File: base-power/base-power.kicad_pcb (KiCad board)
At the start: 2 copper layers, 4 parts

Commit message: Add current sensor, RTC battery, Power protection
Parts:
- removed the P at (52.1, 97.8)
- added 500 mA AC: V***, 2PIN_6mm, F.Cu at (78.7, 87.6)
- added ?: Val**, PIN_ARRAY_1, F.Cu at (99.1, 148.6)
- added Common Choke: VAL**, TRANSF-MICRO, F.Cu at (119.4, 101.6)
- added FUSE: 1,25 A, D3, F.Cu at (100.3, 121.9)
- added INA219: Val**, PIN_ARRAY_5x1, F.Cu at (99.1, 141.0)
- added P: POWER BOARD, VASCH8x2, F.Cu at (363.2, 212.1)
- added P***: BORN2, bornier2, F.Cu at (49.5, 92.7)
- added Power bypass: Val**, PIN_ARRAY_2X1, F.Cu at (95.2, 147.3)
- moved VARISTORE 19.3 mm to (74.9, 115.6), turned to 0 degrees
- moved LD1086 14.2 mm to (76.2, 137.2)
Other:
- board text added: "Gnd"
- board text added: "SCA0"
- board text added: "SCL0"
- board text added: "Scl"
- board text added: "Sda"
- board text added: "Vcc"
- board text added: "Vin+"
- board text added: "Vin-"

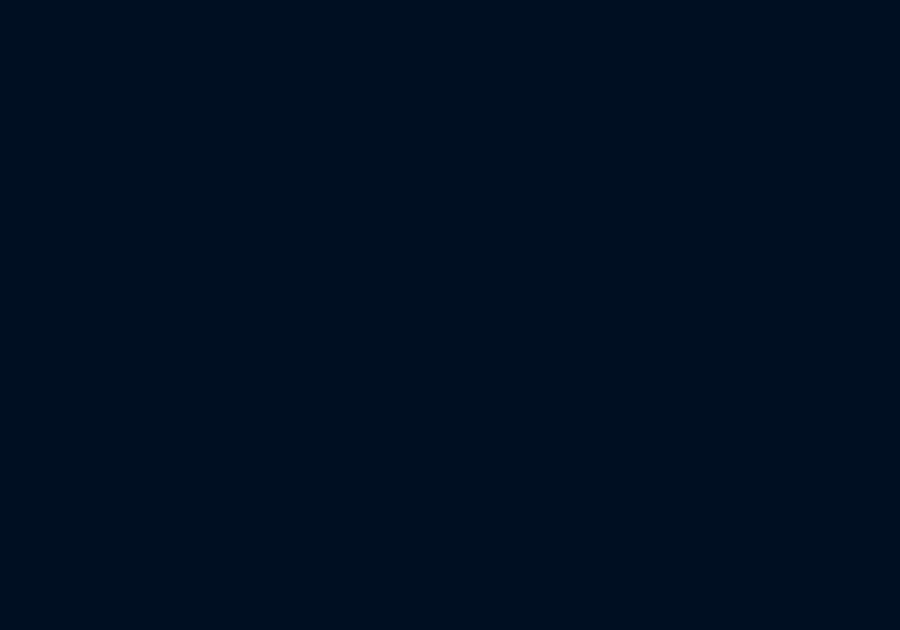
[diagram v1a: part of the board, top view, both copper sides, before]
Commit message: Power revision and add ina219 sensor
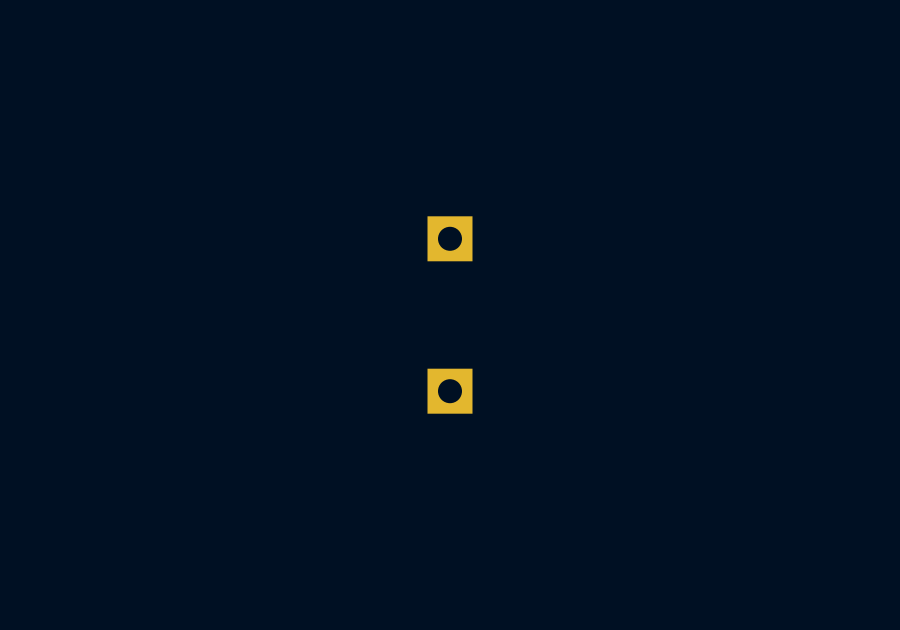
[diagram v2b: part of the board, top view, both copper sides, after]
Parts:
- added AD0: Val**, SIL-1, F.Cu at (340.4, 191.8)
- added AD1: Val**, SIL-1, F.Cu at (340.4, 196.8)
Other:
- board text added: "AD0"
- board text added: "AD1"
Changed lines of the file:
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@@
     (area 43.2816 24.079999 396.290001 262.940001)
     (thickness 1.6)
-    (drawings 21)
+    (drawings 23)
     (tracks 0)
     (zones 0)
-    (modules 11)
+    (modules 13)
     (nets 1)
   )
@@
     (visible_elements FFFFFBBF)
     (pcbplotparams
-      (layerselection 270532608)
+      (layerselection 270565376)
       (usegerberextensions false)
       (excludeedgelayer false)
@@
       (hpglpenoverlay 2)
       (psnegative false)
-      (psa4output false)
+      (psa4output true)
       (plotreference true)
       (plotvalue true)
@@
     (uvia_drill 0.127)
     (add_net "")
+  )
+  (module SIL-1 (layer "Rame Fronte")
+    (at 340.36 196.85)
+    (descr "Connecteurs 1 pin")
+    (tags "CONN DEV")
+    (fp_text reference AD1 (at 0 -1.7) (layer "Serigrafia Fronte")
+      (effects (font (size 0.8 0.8) (thickness 0.15)))
+    )
+    (fp_text value Val** (at 0.1 -1.7) (layer "Serigrafia Fronte") hide
+      (effects (font (size 0.8 0.8) (thickness 0.15)))
+    )
+    (fp_line (start -0.9 -0.9) (end 0.9 -0.9) (layer "Serigrafia Fronte") (width 0.15))
+    (fp_line (start 0.9 -0.9) (end 0.9 0.9) (layer "Serigrafia Fronte") (width 0.15))
+    (fp_line (start 0.9 0.9) (end -0.9 0.9) (layer "Serigrafia Fronte") (width 0.15))
+    (fp_line (start -0.9 0.9) (end -0.9 -0.9) (layer "Serigrafia Fronte") (width 0.15))
+    (pad 1 thru_hole rect (at 0 0) (size 1.5 1.5) (drill 0.8)
+      (layers *.Cu *.Mask "Serigrafia Fronte")
+    )
   )
   (module bornier4 (layer "Rame Fronte")
@@
     )
   )
+  (module SIL-1 (layer "Rame Fronte")
+    (at 340.36 191.77)
+    (descr "Connecteurs 1 pin")
+    (tags "CONN DEV")
+    (fp_text reference AD0 (at 0 -1.7) (layer "Serigrafia Fronte")
+      (effects (font (size 0.8 0.8) (thickness 0.15)))
+    )
+    (fp_text value Val** (at 0.1 -1.7) (layer "Serigrafia Fronte") hide
+      (effects (font (size 0.8 0.8) (thickness 0.15)))
+    )
+    (fp_line (start -0.9 -0.9) (end 0.9 -0.9) (layer "Serigrafia Fronte") (width 0.15))
+    (fp_line (start 0.9 -0.9) (end 0.9 0.9) (layer "Serigrafia Fronte") (width 0.15))
+    (fp_line (start 0.9 0.9) (end -0.9 0.9) (layer "Serigrafia Fronte") (width 0.15))
+    (fp_line (start -0.9 0.9) (end -0.9 -0.9) (layer "Serigrafia Fronte") (width 0.15))
+    (pad 1 thru_hole rect (at 0 0) (size 1.5 1.5) (drill 0.8)
+      (layers *.Cu *.Mask "Serigrafia Fronte")
+    )
+  )
+  (gr_text AD1 (at 372.11 205.74) (layer "Serigrafia Fronte")
+    (effects (font (size 1.5 1.5) (thickness 0.3)))
+  )
+  (gr_text AD0 (at 354.33 205.74) (layer "Serigrafia Fronte")
+    (effects (font (size 1.5 1.5) (thickness 0.3)))
+  )
   (gr_text SCL0 (at 354.33 203.2) (layer "Serigrafia Fronte")

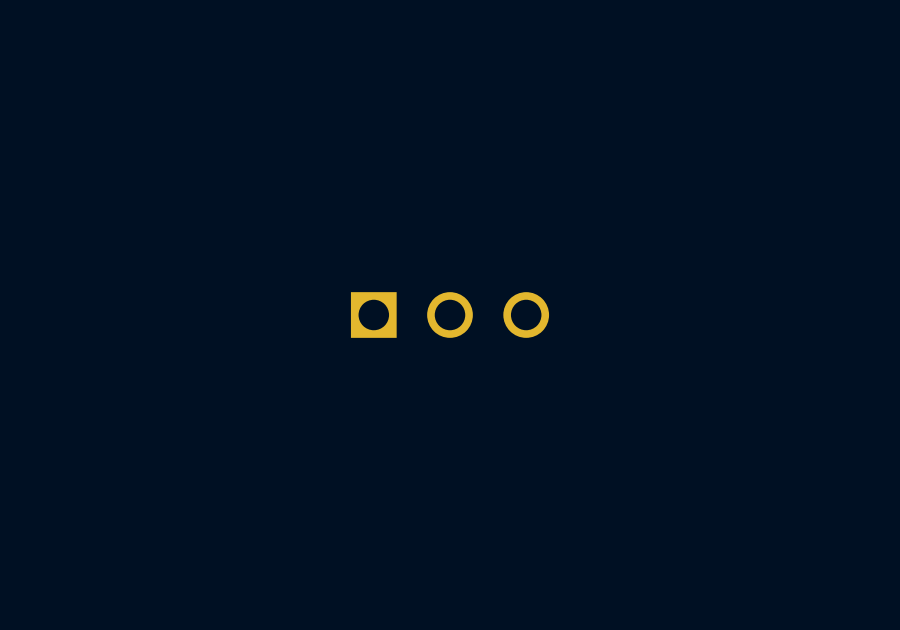
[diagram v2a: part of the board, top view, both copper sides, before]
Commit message: Fix Power schematics
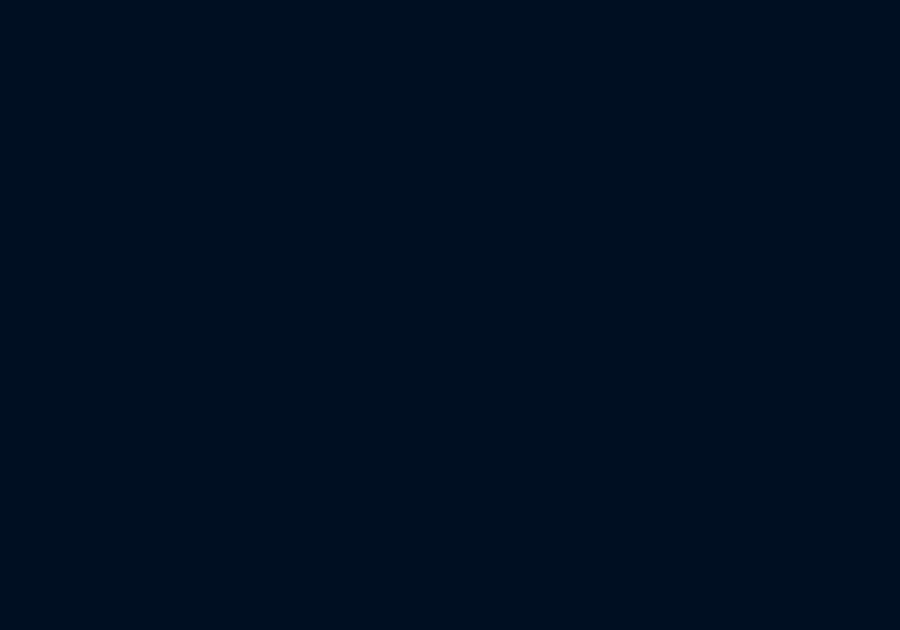
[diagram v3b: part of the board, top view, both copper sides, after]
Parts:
- removed LD1086: Val**, PIN_ARRAY_3X1
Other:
- board text added: "GND 3,3V NC 5V"
- board text removed: "GND 3,3V 3,6V 5V"
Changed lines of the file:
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@@
     (tracks 0)
     (zones 0)
-    (modules 13)
+    (modules 12)
     (nets 1)
   )
@@
     )
   )
-  (module PIN_ARRAY_3X1 (layer "Rame Fronte")
-    (at 76.2 137.16)
-    (descr "Connecteur 3 pins")
-    (tags "CONN DEV")
-    (fp_text reference LD1086 (at 0.254 -2.159) (layer "Serigrafia Fronte")
-      (effects (font (size 1.016 1.016) (thickness 0.1524)))
-    )
-    (fp_text value Val** (at 0 -2.159) (layer "Serigrafia Fronte") hide
-      (effects (font (size 1.016 1.016) (thickness 0.1524)))
-    )
-    (fp_line (start -3.81 1.27) (end -3.81 -1.27) (layer "Serigrafia Fronte") (width 0.1524))
-    (fp_line (start -3.81 -1.27) (end 3.81 -1.27) (layer "Serigrafia Fronte") (width 0.1524))
-    (fp_line (start 3.81 -1.27) (end 3.81 1.27) (layer "Serigrafia Fronte") (width 0.1524))
-    (fp_line (start 3.81 1.27) (end -3.81 1.27) (layer "Serigrafia Fronte") (width 0.1524))
-    (fp_line (start -1.27 -1.27) (end -1.27 1.27) (layer "Serigrafia Fronte") (width 0.1524))
-    (pad 1 thru_hole rect (at -2.54 0) (size 1.524 1.524) (drill 1.016)
-      (layers *.Cu *.Mask "Serigrafia Fronte")
-    )
-    (pad 2 thru_hole circle (at 0 0) (size 1.524 1.524) (drill 1.016)
-      (layers *.Cu *.Mask "Serigrafia Fronte")
-    )
-    (pad 3 thru_hole circle (at 2.54 0) (size 1.524 1.524) (drill 1.016)
-      (layers *.Cu *.Mask "Serigrafia Fronte")
-    )
-    (model pin_array/pins_array_3x1.wrl
-      (at (xyz 0 0 0))
-      (scale (xyz 1 1 1))
-      (rotate (xyz 0 0 0))
-    )
-  )
   (module PIN_ARRAY_2X1 (layer "Rame Fronte")
     (at 74.93 115.57)
@@
     )
   )
+  (gr_text "GND 3,3V NC 5V" (at 354.33 247.65) (layer "Serigrafia Fronte")
+    (effects (font (size 1.5 1.5) (thickness 0.3)))
+  )
   (gr_text AD1 (at 372.11 205.74) (layer "Serigrafia Fronte")
     (effects (font (size 1.5 1.5) (thickness 0.3)))
@@
   (gr_line (start 88.9 119.38) (end 88.9 132.08) (angle 90) (layer "Serigrafia Fronte") (width 0.2))
   (gr_line (start 64.77 119.38) (end 88.9 119.38) (angle 90) (layer "Serigrafia Fronte") (width 0.2))
-  (gr_text "GND 3,3V 3,6V 5V" (at 354.33 247.65) (layer "Serigrafia Fronte")
-    (effects (font (size 1.5 1.5) (thickness 0.3)))
-  )
   (gr_line (start 45.72 76.2) (end 48.26 76.2) (angle 90) (layer "Contorno scheda") (width 0.1))
   (gr_line (start 45.72 262.89) (end 45.72 76.2) (angle 90) (layer "Contorno scheda") (width 0.1))
